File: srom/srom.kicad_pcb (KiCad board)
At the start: 2 copper layers, 116.8 x 118.9 mm, 95 parts, among them J1 Conn_01x03_Female, J201 Conn_01x03_Female, J301 Conn_01x05_Female, J302 Conn_01x04_Female, J303 Conn_01x03_Female, Q1 PMBT2222A, U1 4075, U201 Pico-2 IO, U202 74LS245, U301 Pico-3 UI, U4 74LS245, U5 Pico-1 ROM

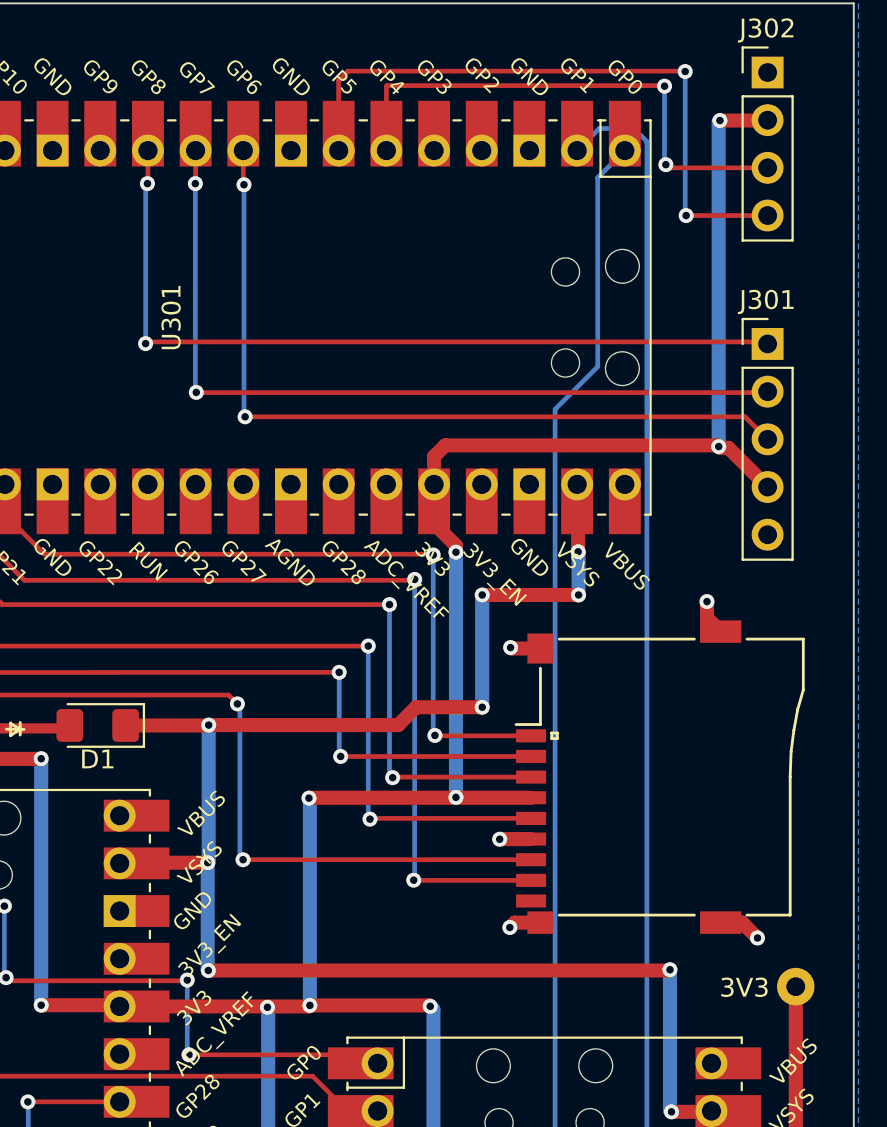
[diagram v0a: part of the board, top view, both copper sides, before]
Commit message: break out the 3V3 supplies into separate ones
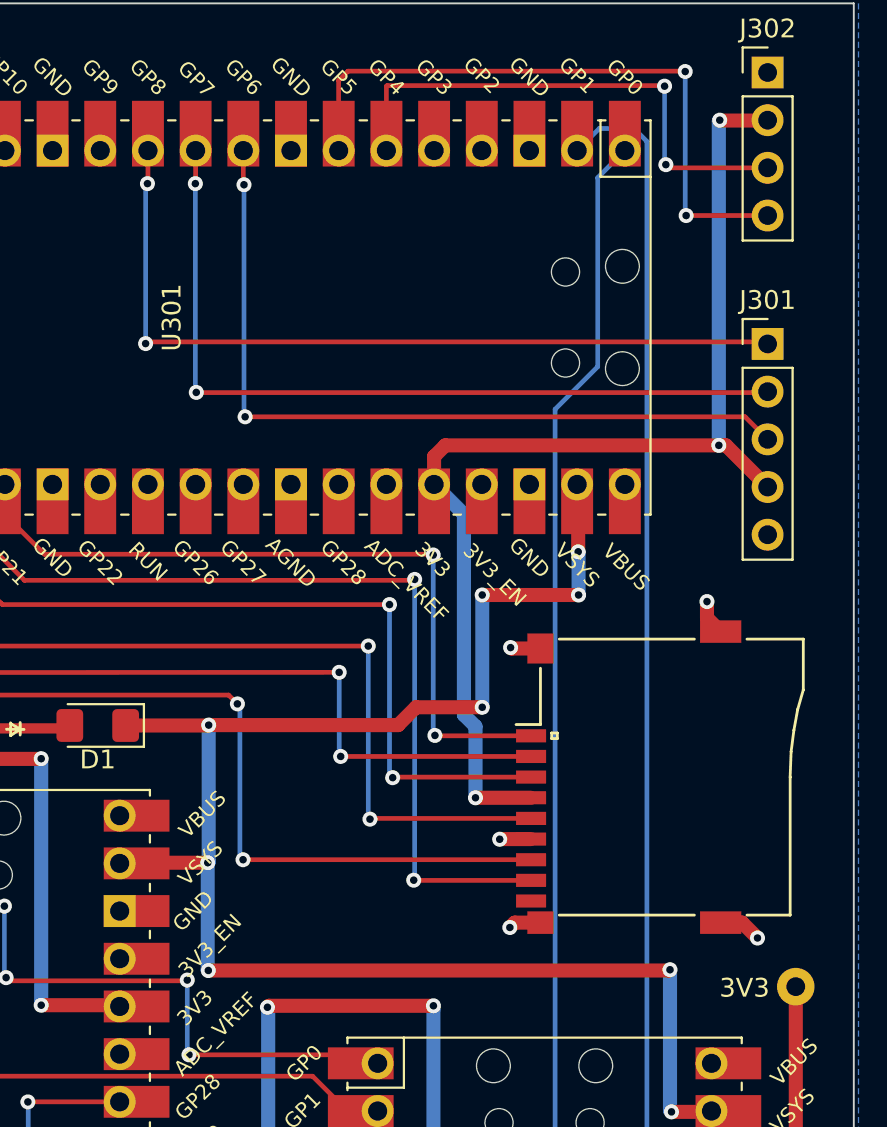
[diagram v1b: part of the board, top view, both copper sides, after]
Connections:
- ? pad : +3V3 -> 3V3_PICO2
- C1 pad 1: +3V3 -> 3V3_PICO1
- C201 pad 2: +3V3 -> 3V3_PICO2
- J301 pad 4: +3V3 -> 3V3_PICO3
- J302 pad 2: +3V3 -> 3V3_PICO3
- U201 pad 36: +3V3 -> 3V3_PICO2
- U202 pad 1: +3V3 -> 3V3_PICO2
- U202 pad 20: +3V3 -> 3V3_PICO2
- U301 pad 36: +3V3 -> 3V3_PICO3
- U4 pad 20: +3V3 -> 3V3_PICO1
- U5 pad 36: +3V3 -> 3V3_PICO1
- XS301 pad 4: +3V3 -> 3V3_PICO3
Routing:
- net +3V3: track 261.8 -> 0.00 mm, vias 12 -> 0
- net 3V3_PICO2: track 0.00 -> 119.0 mm, vias 0 -> 4
- net 3V3_PICO3: track 0.00 -> 60.8 mm, vias 0 -> 3
- net 3V3_PICO1: track 0.00 -> 56.9 mm, vias 0 -> 2

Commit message: first draft of layout of board 2
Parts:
- removed 10 (x6), 11 (x6), 12 (x6), 13 (x6), 14 (x6), 5 (x6), 6 (x6), 7 (x6), 8 (x6), 9 (x6), ? (x8): , 
- added C101: C_Small, Capacitor_SMD:C_1206_3216Metric, F.Cu at (91.5, 138.7)
- added U101: 74LS245, Package_SO:SO-20_5.3x12.6mm_P1.27mm, F.Cu at (83.8, 139.6)
- U202: value 74LS245 -> APS6404L-3SQR_PSRAM64Mbit; footprint Package_SO:SO-20_5.3x12.6mm_P1.27mm -> Package_SO:SOIC-8_3.9x4.9mm_P1.27mm
- moved U202 62.9 mm to (133.2, 103.5)
- moved C201 58.9 mm to (132.0, 98.0)
- moved Q1 26.6 mm to (121.7, 161.6)
- moved R1 26.0 mm to (126.7, 161.0), turned to -90 degrees
- moved C3 8.03 mm to (85.9, 115.9), turned to 0 degrees
- moved J1 4.04 mm to (113.1, 156.5)
- moved U5 3.66 mm to (110.6, 122.7)
- moved U4 3.42 mm to (83.6, 105.4)
- moved R101 3.28 mm to (93.1, 98.5)
- moved R102 3.28 mm to (93.1, 100.9)
- moved R103 3.28 mm to (93.1, 103.3)
- moved R104 3.28 mm to (93.1, 105.7)
- moved R105 3.28 mm to (93.1, 108.1)
- moved R106 3.28 mm to (93.1, 110.5)
- moved R107 3.28 mm to (93.1, 112.9)
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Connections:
- net MISO_D0 renamed SPI0_SD_MISO
- net MOSI_DI renamed SPI0_SD_MOSI
- net SD_CLK renamed SPI0_SD_CLK
- net SD_SS renamed SPI0_SD_SLAVE_ENABLE
- C201 pad 1: GND -> 3V3_PICO2
- C201 pad 2: 3V3_PICO2 -> GND
- R104 pad 2: D5 -> D3
- R105 pad 2: D3 -> D4
- R106 pad 2: D6 -> D5
- R107 pad 2: D4 -> D6
- U201 pad 11: IORQ -> IF1_PORT_ACTIVE
- U201 pad 12: RD -> ZXA3
- U201 pad 14: WR -> unconnected-(U201-Pad14)
- U201 pad 15: ZXA0 -> unconnected-(U201-Pad15)
- U201 pad 16: ZXA1 -> SPI1_UI_MOSI
- U201 pad 17: ZXA2 -> SPI1_UI_SLAVE_ENABLE
- U201 pad 19: ZXA3 -> SPI1_UI_CLK
- U201 pad 20: unconnected-(U201-Pad20) -> SPI1_UI_MISO
- U201 pad 21: UI_PICO_TX -> SPI0_PSRAM_MISO
- U201 pad 22: UI_PICO_RX -> ROM_READ_INV_3V3
- U201 pad 24: unconnected-(U201-Pad24) -> SPI0_PSRAM_CLK
- U201 pad 25: unconnected-(U201-Pad25) -> SPI0_PSRAM_MOSI
- U201 pad 26: ZXA4 -> ZXIORQ
- U201 pad 27: ZXA5 -> ZXRD
- U201 pad 29: ZXA6 -> ZXWR
- U201 pad 31: ZXA7 -> SPI0_PSRAM_SLAVE_ENABLE
- U201 pad 32: unconnected-(U201-Pad32) -> ZXWAIT
- U201 pad 34: unconnected-(U201-Pad34) -> DBUS_DIRECTION
- U201 pad 5: D5 -> D3
- U201 pad 6: D3 -> D4
- U201 pad 7: D6 -> D5
- U201 pad 9: D4 -> D6
- U202 pad 1: 3V3_PICO2 -> SPI0_PSRAM_SLAVE_ENABLE
- U202 pad 2: ZXIORQ -> SPI0_PSRAM_MISO
- U202 pad 3: ZXRD -> unconnected-(U202-Pad3)
- U202 pad 4: ZXWR -> GND
- U202 pad 5: unconnected-(U202-Pad5) -> SPI0_PSRAM_MOSI
- U202 pad 6: unconnected-(U202-Pad6) -> SPI0_PSRAM_CLK
- U202 pad 8: unconnected-(U202-Pad8) -> 3V3_PICO2
- U301 pad 1: UI_PICO_TX -> unconnected-(U301-Pad1)
- U301 pad 16: unconnected-(U301-Pad16) -> SPI1_UI_MISO
- U301 pad 17: unconnected-(U301-Pad17) -> SPI1_UI_SLAVE_ENABLE
- U301 pad 19: unconnected-(U301-Pad19) -> SPI1_UI_CLK
- U301 pad 2: UI_PICO_RX -> unconnected-(U301-Pad2)
- U301 pad 20: unconnected-(U301-Pad20) -> SPI1_UI_MOSI
- U301 pad 26: SD_DAT1 -> unconnected-(U301-Pad26)
- U301 pad 27: SD_DAT2 -> unconnected-(U301-Pad27)
- U4 pad 1: ROM_READ_INV -> DBUS_DIRECTION
- U4 pad 5: ZXD5 -> ZXD3
- U4 pad 6: ZXD3 -> ZXD4
- U4 pad 7: ZXD6 -> ZXD5
- U4 pad 8: ZXD4 -> ZXD6
- U5 pad 11: ROM_READ_INV -> ZXA0
- U5 pad 12: ZXA13 -> ZXA1
- U5 pad 14: ZXA12 -> ZXA2
- U5 pad 15: ZXA0 -> ZXA3
- U5 pad 16: ZXA1 -> ZXA4
- U5 pad 17: ZXA2 -> ZXA5
- U5 pad 19: ZXA3 -> ZXA6
- U5 pad 20: ZXM1 -> ZXA7
- U5 pad 21: ZXA11 -> ZXA8
- U5 pad 22: ZXA10 -> ZXA9
- U5 pad 24: ZXA9 -> ZXA10
- U5 pad 25: ZXA8 -> ZXA11
- U5 pad 26: ZXA4 -> ZXA12
- U5 pad 27: ZXA5 -> ZXA13
- U5 pad 29: ZXA6 -> ZXM1
- U5 pad 31: ZXA7 -> ROM_READ_INV_3V3
- U5 pad 32: unconnected-(U5-Pad32) -> IF1_PORT_ACTIVE
- U5 pad 5: D5 -> D3
- U5 pad 6: D3 -> D4
- U5 pad 7: D6 -> D5
- U5 pad 9: D4 -> D6
- XS301 pad 1: SD_DAT2 -> unconnected-(XS301-Pad1)
- XS301 pad 8: SD_DAT1 -> unconnected-(XS301-Pad8)
- Z1 pad A21: unconnected-(Z1-PadA21) -> ZXWAIT
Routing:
- net SPI1_UI_MOSI: track 0.00 -> 132.8 mm, vias 0 -> 7
- net SPI1_UI_CLK: track 0.00 -> 129.4 mm, vias 0 -> 5
- net ZXWAIT: track 0.00 -> 125.3 mm, vias 0 -> 4
- net SPI1_UI_SLAVE_ENABLE: track 0.00 -> 123.5 mm, vias 0 -> 5
- net SPI1_UI_MISO: track 0.00 -> 121.6 mm, vias 0 -> 5
- net DBUS_DIRECTION: track 0.00 -> 119.5 mm, vias 0 -> 6
- net UI_PICO_RX: track 111.5 -> 0.00 mm, vias 1 -> 0
- net UI_PICO_TX: track 108.9 -> 0.00 mm, vias 1 -> 0
- net ROM_READ_INV_3V3: track 0.00 -> 106.2 mm, vias 0 -> 4
- net ZXA7: track 156.2 -> 65.8 mm, vias 10 -> 4
- net ZXA6: track 152.2 -> 63.1 mm, vias 8 -> 7
- net SPI0_PSRAM_MISO: track 0.00 -> 85.5 mm, vias 0 -> 4
- net ZXA5: track 145.1 -> 62.9 mm, vias 8 -> 4
- net 3V3_PICO2: track 119.0 -> 44.4 mm
- net ZXA4: track 143.6 -> 69.3 mm, vias 10 -> 4
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- removed copper zone on F.Cu, net GND
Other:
- board text added: "github.com/derekfountain/zx-spectrum-pico-if1 v1.3"
- board text removed: "github.com/derekfountain/zx-spectrum-pico-if1 v1.1"

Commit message: more work on the layout of board 2
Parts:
- added J101: Conn_01x06_Female, Connector_PinHeader_2.54mm:PinHeader_1x06_P2.54mm_Vertical, F.Cu at (132.2, 171.7)
- added J202: Conn_01x05_Female, Connector_PinHeader_2.54mm:PinHeader_1x05_P2.54mm_Vertical, F.Cu at (144.8, 171.5)
- added REF**: R_1206_3216Metric_Pad1.30x1.75mm_HandSolder, Resistor_SMD:R_1206_3216Metric_Pad1.30x1.75mm_HandSolder, F.Cu at (93.8, 129.6)
- moved XS301 2.47 mm to (158.0, 97.4)
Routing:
- net DBUS_DIRECTION: track 119.5 -> 190.8 mm, vias 6 -> 11
- net ZXA3: track 102.5 -> 147.2 mm, vias 6 -> 9
- net IF1_PORT_ACTIVE: track 35.9 -> 72.9 mm, vias 2 -> 4
- net ZXWR: track 115.9 -> 150.9 mm, vias 4 -> 7
- net ZXIORQ: track 119.0 -> 153.9 mm, vias 4 -> 7
- net ZXWAIT: track 125.3 -> 157.9 mm, vias 4 -> 7
- net ZXM1: track 91.5 -> 116.8 mm, vias 2 -> 5
- net ROM_READ_INV_3V3: track 106.2 -> 129.4 mm, vias 4 -> 6
- net ZXRD: track 156.3 -> 179.2 mm
- net ZXRESET: track 90.0 -> 108.3 mm, vias 4 -> 6
- net PICO_RESET_Z80: track 52.9 -> 70.6 mm, vias 2 -> 5
- net SPI1_UI_SLAVE_ENABLE: track 123.5 -> 119.5 mm
- net ROM_READ_INV: track 25.6 -> 29.5 mm
- net 3V3_PICO3: track 61.9 -> 64.4 mm
- net SPI0_SD_MOSI: track 46.6 -> 49.1 mm
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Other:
- board text added: "*"
- board text added: "A3"
- board text added: "Add test points to SPI buses I can add a test blipper on Pico2 Add a test blipper to Pico3 Add a couple of ground points, a couple of 3V3 points and a 5V"
- board text added: "DIR"
- board text added: "IF1IO"
- board text added: "M1"
- board text added: "NOPOP"
- board text added: "PRST"
- board text added: "ROMRD"
- board text added: "WAIT"
- board text added: "Z80RST"
- board text removed: "5V"
- board text removed: "GND"
- board text removed: "RX"
- board text removed: "TX"

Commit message: v1.3 of the board off to production
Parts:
- added ?: , , F.Cu at (159.3, 124.1)
- added ?: , , F.Cu at (124.6, 59.3)
- added ?: , , F.Cu at (97.5, 88.3)
- added ?: , , F.Cu at (97.6, 85.5)
- added ?: , , F.Cu at (91.2, 63.9)
- added ?: , , F.Cu at (111.4, 170.9)
- added ?: , , F.Cu at (93.8, 63.9)
- added ?: , , F.Cu at (97.6, 82.8)
- added ?: , , F.Cu at (159.3, 121.5)
- added ?: , , F.Cu at (88.7, 75.6)
- added ?: , , F.Cu at (88.4, 63.8)
- added ?: , , F.Cu at (159.0, 150.7)
- added ?: , , F.Cu at (129.7, 59.2)
- added ?: , , F.Cu at (159.1, 160.8)
- added ?: , , F.Cu at (159.0, 135.5)
- added ?: , , F.Cu at (159.0, 153.3)
- added ?: , , F.Cu at (135.0, 88.7)
- added ?: , , F.Cu at (159.2, 117.7)
- added ?: , , F.Cu at (127.1, 59.3)
- added ?: , , F.Cu at (97.7, 80.1)
- added ?: , , F.Cu at (88.4, 66.8)
- added ?: , , F.Cu at (96.6, 64.0)
- added ?: , , F.Cu at (137.3, 59.3)
- added ?: , , F.Cu at (134.6, 59.3)
- added ?: , , F.Cu at (137.5, 88.7)
- added ?: , , F.Cu at (93.5, 119.7)
- J202: value Conn_01x05_Female -> Conn_01x06_Female; footprint Connector_PinHeader_2.54mm:PinHeader_1x05_P2.54mm_Vertical -> Connector_PinHeader_2.54mm:PinHeader_1x06_P2.54mm_Vertical
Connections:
- U201 pad 14: unconnected-(U201-Pad14) -> TEST_BLIPPER_P2
- U301 pad 14: unconnected-(U301-Pad14) -> TEST_BLIPPER_P3
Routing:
- net TEST_BLIPPER_P2: track 0.00 -> 46.4 mm, vias 0 -> 5
- net TEST_BLIPPER_P3: track 0.00 -> 39.5 mm, vias 0 -> 2
- net SPI1_UI_MISO: track 121.6 -> 149.5 mm
- net SPI1_UI_SLAVE_ENABLE: track 119.5 -> 141.8 mm
- net SPI0_SD_MOSI: track 49.1 -> 64.5 mm
- net SPI1_UI_CLK: track 129.6 -> 144.1 mm
- net SPI0_SD_CLK: track 52.9 -> 66.3 mm
- net 3V3_PICO3: track 64.4 -> 75.0 mm
- net 3V3_PICO2: track 44.4 -> 54.8 mm
- net SPI0_SD_SLAVE_ENABLE: track 55.3 -> 64.4 mm
- net +5V: track 171.2 -> 179.9 mm
- net GND: track 98.9 -> 107.5 mm, vias 21 -> 22
- net SPI0_SD_MISO: track 61.8 -> 67.6 mm
- net SPI1_UI_MOSI: track 132.8 -> 137.9 mm
- net OLED_SDA: track 25.7 -> 30.4 mm
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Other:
- board text added: "5V"
- board text added: "CLK"
- board text added: "GND"
- board text added: "MISO"
- board text added: "MOSI"
- board text added: "SD_CLK"
- board text added: "SD_MISO"
- board text added: "SD_MOSI"
- board text added: "SD_SLAVE_EN"
- board text added: "SLAVE EN"
- board text added: "TST"
- board text removed: "Add test points to SPI buses I can add a test blipper on Pico2 Add a test blipper to Pico3 Add a couple of ground points, a couple of 3V3 points and a 5V"
